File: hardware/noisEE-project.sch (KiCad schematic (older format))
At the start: 109 parts, among them IC1 ATTINY84-S, J1 VOL_CONN, J2 Stereo_CONN, J3 COLOR_CONN, J4 USB_OTG, P2 ISP_02x03, Q1 PN2222A, Q2 PN2222A, SW1 SW_DIP_x01, U1 LMH6642(SOT23)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

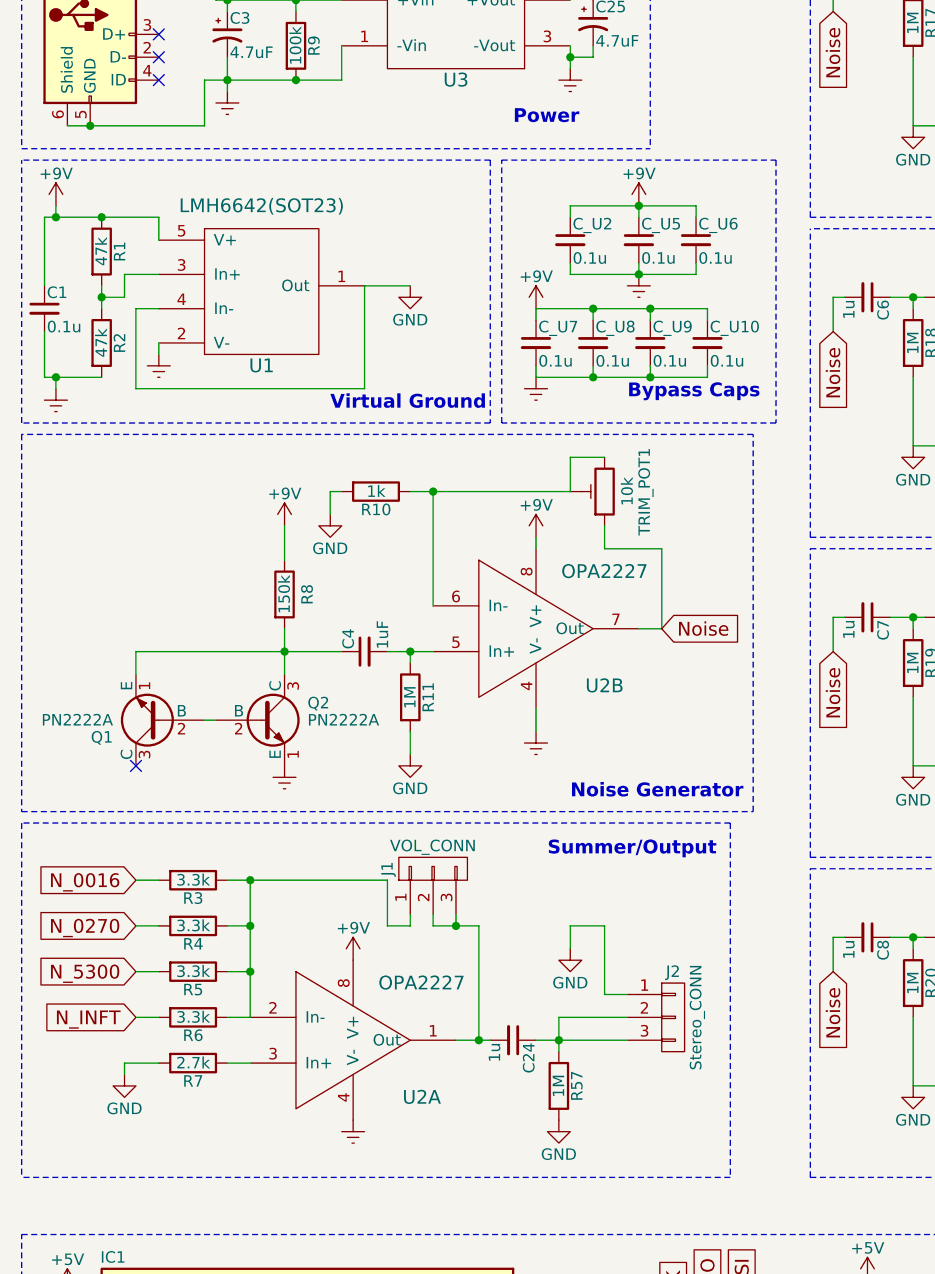
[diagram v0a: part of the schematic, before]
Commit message: Use two opamps for pre-amp and output stages, clean up board and lay down tracks for all signal paths
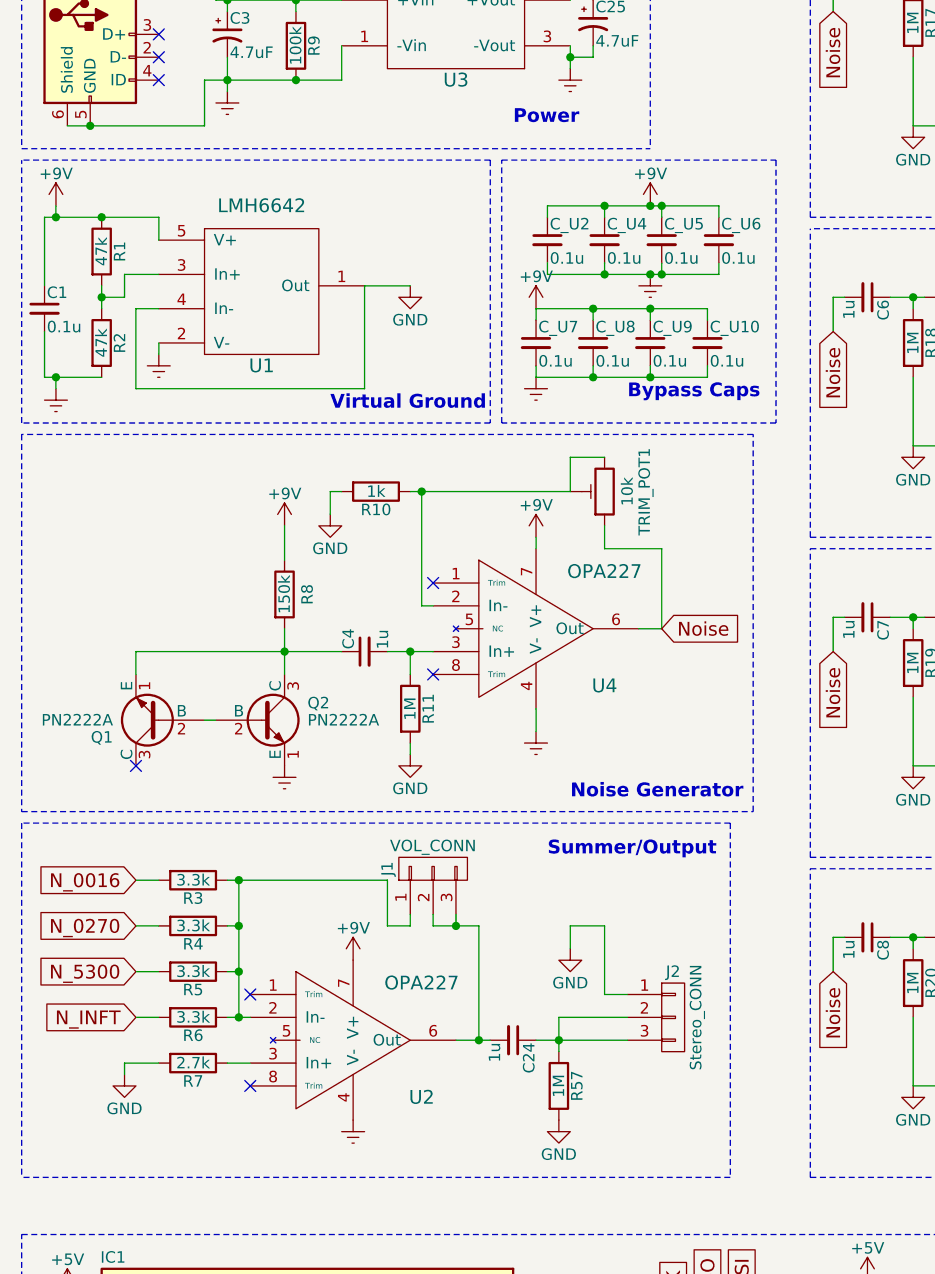
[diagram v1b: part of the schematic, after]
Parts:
- removed U2: OPA2227, Housings_SOIC:SOIC-8_3.9x4.9mm_Pitch1.27mm, symbol OPA2227
- added C_U4: 0.1u, Capacitors_SMD:C_0805, symbol C_Small
- added U2, U4: OPA227, Housings_SOIC:SOIC-8_3.9x4.9mm_Pitch1.27mm, symbol OPA227
- C4: value 1uF -> 1u
- U1: value LMH6642(SOT23) -> LMH6642
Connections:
- net +9V: now also C_U4.1, U2.7 (V+), U4.7 (V+)
- net Earth: now also C_U4.2, U2.4 (V-), U4.4 (V-)
- net Noise: now also U4.6 (Out)
- net at C4.2, R11.1: now also U4.3 (In+)
- net at R10.1, TRIM_POT1.2, TRIM_POT1.3: now also U4.2 (In-)
- net at C24.2, J1.2 (P2), J1.3 (P3): now also U2.6 (Out)
- net at J1.1 (P1), R3.1, R4.1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: now also U2.2 (In-)
- net at R7.1: now also U2.3 (In+)
- no-connect marks 4 -> 8
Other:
- moved on the sheet: C_U2, C_U5, C_U6, R11
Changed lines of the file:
@@
 P 1550 2150
 F 0 "U1" H 1550 1800 60  0000 C CNN
-F 1 "LMH6642(SOT23)" H 1550 2500 60  0000 C CNN
+F 1 "LMH6642" H 1550 2500 60  0000 C CNN
 F 2 "TO_SOT_Packages_SMD:SOT-23-5" H 1550 2150 60  0001 C CNN
 F 3 "" H 1550 2150 60  0001 C CNN
@@
 P 2000 3750
 F 0 "C4" H 2010 3820 50  0000 L CNN
-F 1 "1uF" H 2010 3670 50  0000 L CNN
+F 1 "1u" H 2010 3670 50  0000 L CNN
 F 2 "Capacitors_SMD:C_0805" H 2000 3750 50  0001 C CNN
 F 3 "" H 2000 3750 50  0000 C CNN
@@
 $EndComp
 $Comp
-L OPA2227 U2
-U 2 1 58A176E6
-P 2650 3650
-F 0 "U2" H 3050 3400 60  0000 C CNN
-F 1 "OPA2227" H 3050 3900 60  0000 C CNN
-F 2 "Housings_SOIC:SOIC-8_3.9x4.9mm_Pitch1.27mm" H 2650 3650 60  0001 C CNN
-F 3 "" H 2650 3650 60  0001 C CNN
-	2    2650 3650
-	1    0    0    -1
-$EndComp
-$Comp
 L R R10
 U 1 1 58A178E2
@@
 L R R11
 U 1 1 58A18310
-P 2200 3950
-F 0 "R11" V 2280 3950 50  0000 C CNN
-F 1 "1M" V 2200 3950 50  0000 C CNN
-F 2 "Resistors_SMD:R_0805" V 2130 3950 50  0001 C CNN
-F 3 "" H 2200 3950 50  0000 C CNN
-	1    2200 3950
+P 2200 4000
+F 0 "R11" V 2280 4000 50  0000 C CNN
+F 1 "1M" V 2200 4000 50  0000 C CNN
+F 2 "Resistors_SMD:R_0805" V 2130 4000 50  0001 C CNN
+F 3 "" H 2200 4000 50  0000 C CNN
+	1    2200 4000
 	1    0    0    -1
 $EndComp
@@
 N_0016
 $Comp
-L OPA2227 U2
-U 1 1 58A24451
-P 1850 5450
-F 0 "U2" H 2250 5200 60  0000 C CNN
-F 1 "OPA2227" H 2250 5700 60  0000 C CNN
-F 2 "Housings_SOIC:SOIC-8_3.9x4.9mm_Pitch1.27mm" H 1850 5450 60  0001 C CNN
-F 3 "" H 1850 5450 60  0001 C CNN
-	1    1850 5450
-	1    0    0    -1
-$EndComp
-$Comp
 L +9V #PWR019
 U 1 1 58A2555B
@@
 L +9V #PWR087
 U 1 1 58E53024
-P 3200 1800
-F 0 "#PWR087" H 3200 1650 50  0001 C CNN
-F 1 "+9V" H 3200 1940 50  0000 C CNN
-F 2 "" H 3200 1800 50  0000 C CNN
-F 3 "" H 3200 1800 50  0000 C CNN
-	1    3200 1800
+P 3250 1800
+F 0 "#PWR087" H 3250 1650 50  0001 C CNN
+F 1 "+9V" H 3250 1940 50  0000 C CNN
+F 2 "" H 3250 1800 50  0000 C CNN
+F 3 "" H 3250 1800 50  0000 C CNN
+	1    3250 1800
 	1    0    0    -1
 $EndComp
@@
 L Earth #PWR088
 U 1 1 58E5317F
-P 3200 2100
-F 0 "#PWR088" H 3200 1850 50  0001 C CNN
-F 1 "Earth" H 3200 1950 50  0001 C CNN
-F 2 "" H 3200 2100 50  0000 C CNN
-F 3 "" H 3200 2100 50  0000 C CNN
-	1    3200 2100
+P 3250 2100
+F 0 "#PWR088" H 3250 1850 50  0001 C CNN
+F 1 "Earth" H 3250 1950 50  0001 C CNN
+F 2 "" H 3250 2100 50  0000 C CNN
+F 3 "" H 3250 2100 50  0000 C CNN
+	1    3250 2100
 	1    0    0    -1
 $EndComp
@@
 L C_Small C_U2
 U 1 1 58E5342B
-P 2900 1950
-F 0 "C_U2" H 2910 2020 50  0000 L CNN
-F 1 "0.1u" H 2910 1870 50  0000 L CNN
-F 2 "Capacitors_SMD:C_0805" H 2900 1950 50  0001 C CNN
-F 3 "" H 2900 1950 50  0000 C CNN
-	1    2900 1950
+P 2800 1950
+F 0 "C_U2" H 2810 2020 50  0000 L CNN
+F 1 "0.1u" H 2810 1870 50  0000 L CNN
+F 2 "Capacitors_SMD:C_0805" H 2800 1950 50  0001 C CNN
+F 3 "" H 2800 1950 50  0000 C CNN
+	1    2800 1950
 	1    0    0    -1
 $EndComp
@@
 L C_Small C_U5
 U 1 1 58E5803C
-P 3200 1950
-F 0 "C_U5" H 3210 2020 50  0000 L CNN
-F 1 "0.1u" H 3210 1870 50  0000 L CNN
-F 2 "Capacitors_SMD:C_0805" H 3200 1950 50  0001 C CNN
-F 3 "" H 3200 1950 50  0000 C CNN
-	1    3200 1950
+P 3300 1950
+F 0 "C_U5" H 3310 2020 50  0000 L CNN
+F 1 "0.1u" H 3310 1870 50  0000 L CNN
+F 2 "Capacitors_SMD:C_0805" H 3300 1950 50  0001 C CNN
+F 3 "" H 3300 1950 50  0000 C CNN
+	1    3300 1950
 	1    0    0    -1
 $EndComp
@@
 L C_Small C_U6
 U 1 1 58E5F42C
-P 3450 1950
-F 0 "C_U6" H 3460 2020 50  0000 L CNN
-F 1 "0.1u" H 3460 1870 50  0000 L CNN
-F 2 "Capacitors_SMD:C_0805" H 3450 1950 50  0001 C CNN
-F 3 "" H 3450 1950 50  0000 C CNN
-	1    3450 1950
+P 3550 1950
+F 0 "C_U6" H 3560 2020 50  0000 L CNN
+F 1 "0.1u" H 3560 1870 50  0000 L CNN
+F 2 "Capacitors_SMD:C_0805" H 3550 1950 50  0001 C CNN
+F 3 "" H 3550 1950 50  0000 C CNN
+	1    3550 1950
 	1    0    0    -1
 $EndComp
@@
 Wire Wire Line
 	2200 3050 2900 3050
-Connection ~ 2300 3050
 Wire Wire Line
 	2100 3750 2300 3750
@@
 Connection ~ 2200 3750
 Wire Wire Line
-	1500 4750 1500 5350
-Wire Wire Line
-	1400 4950 1500 4950
-Connection ~ 1500 4950
-Wire Wire Line
-	1400 5150 1500 5150
-Connection ~ 1500 5150
-Wire Wire Line
 	1500 5350 1400 5350
-Connection ~ 1500 4750
 Connection ~ 2500 5450
 Wire Wire Line
@@
 Connection ~ 1700 1250
 Wire Wire Line
-	2200 3750 2200 3800
-Wire Wire Line
-	2200 4100 2200 4200
-Wire Wire Line
 	3050 3200 3050 3300
 Wire Wire Line
@@
 	2900 3050 2900 2900
 Wire Wire Line
-	2300 3050 2300 3550
-Wire Wire Line
 	4050 950  4050 800
 Wire Wire Line
@@
 	600  1850 600  2150
 Wire Wire Line
-	3200 1800 3200 1850
-Wire Wire Line
-	2900 1800 3450 1800
-Wire Wire Line
-	3450 1800 3450 1850
-Wire Wire Line
-	2900 1800 2900 1850
-Connection ~ 3200 1800
-Wire Wire Line
-	2900 2050 2900 2100
-Wire Wire Line
-	2900 2100 3450 2100
-Wire Wire Line
-	3200 2100 3200 2050
-Wire Wire Line
-	3450 2100 3450 2050
-Connection ~ 3200 2100
-Wire Wire Line
 	2750 2250 2750 2300
 Wire Wire Line
@@
 	2100 4750 2100 4950
 Wire Wire Line
-	2100 4750 1400 4750
-Wire Wire Line
 	2100 4950 2200 4950
 Wire Wire Line
@@
 Connection ~ 800  1450
 NoConn ~ 1100 1250
+$Comp
+L OPA227 U2
+U 1 1 58C4BAC6
+P 1850 5450
+F 0 "U2" H 2250 5200 60  0000 C CNN
+F 1 "OPA227" H 2250 5700 60  0000 C CNN
+F 2 "Housings_SOIC:SOIC-8_3.9x4.9mm_Pitch1.27mm" H 1850 5450 60  0001 C CNN
+F 3 "" H 1850 5450 60  0001 C CNN
+	1    1850 5450
+	1    0    0    -1
+$EndComp
+Wire Wire Line
+	2100 4750 1400 4750
+Wire Wire Line
+	1450 4750 1450 5350
+Connection ~ 1450 5350
+Connection ~ 1450 4750
+Wire Wire Line
+	1450 5150 1400 5150
+Connection ~ 1450 5150
+Wire Wire Line
+	1450 4950 1400 4950
+Connection ~ 1450 4950
+NoConn ~ 1500 5650
+NoConn ~ 1500 5250
+$Comp
+L OPA227 U4
+U 1 1 58C52F90
+P 2650 3650
+F 0 "U4" H 3050 3400 60  0000 C CNN
+F 1 "OPA227" H 3050 3900 60  0000 C CNN
+F 2 "Housings_SOIC:SOIC-8_3.9x4.9mm_Pitch1.27mm" H 2650 3650 60  0001 C CNN
+F 3 "" H 2650 3650 60  0001 C CNN
+	1    2650 3650
+	1    0    0    -1
+$EndComp
+Wire Wire Line
+	2200 3850 2200 3750
+Wire Wire Line
+	2200 4150 2200 4200
+NoConn ~ 2300 3850
+NoConn ~ 2300 3450
+Connection ~ 2250 3050
+Wire Wire Line
+	2300 3550 2250 3550
+$Comp
+L C_Small C_U4
+U 1 1 58C5D92D
+P 3050 1950
+F 0 "C_U4" H 3060 2020 50  0000 L CNN
+F 1 "0.1u" H 3060 1870 50  0000 L CNN
+F 2 "Capacitors_SMD:C_0805" H 3050 1950 50  0001 C CNN
+F 3 "" H 3050 1950 50  0001 C CNN
+	1    3050 1950
+	1    0    0    -1
+$EndComp
+Wire Wire Line
+	2800 1850 2800 1800
+Wire Wire Line
+	3550 1800 3550 1850
+Wire Wire Line
+	3300 1800 3300 1850
+Connection ~ 3250 1800
+Wire Wire Line
+	3050 1800 3050 1850
+Connection ~ 3050 1800
+Wire Wire Line
+	2800 1800 3550 1800
+Connection ~ 3300 1800
+Wire Wire Line
+	3550 2100 3550 2050
+Wire Wire Line
+	2800 2100 3550 2100
+Wire Wire Line
+	3300 2050 3300 2100
+Connection ~ 3300 2100
+Wire Wire Line
+	3050 2050 3050 2100
+Connection ~ 3250 2100
+Wire Wire Line
+	2800 2050 2800 2100
+Connection ~ 3050 2100
+Wire Wire Line
+	2250 3550 2250 3050
 $EndSCHEMATC

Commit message: Split up the ground (GND->VCOM)
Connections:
- net GND renamed VCOM

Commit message: Check in v2 hardware with fixes for USI and AD5292 Vss issues
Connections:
- net Earth: now also U10.9 (GND), U7.9 (GND), U8.9 (GND), U9.9 (GND)
- net SPI_MISO: now also R16.2; no longer R15.2, R58.2
- net SPI_MOSI: now also R15.2, R58.2; no longer R16.2
- net VCOM: no longer U10.9 (GND), U7.9 (GND), U8.9 (GND), U9.9 (GND)
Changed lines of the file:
@@
 Text GLabel 4250 6850 2    60   Input ~ 0
 SPI_CLK
+Text GLabel 4250 7250 2    60   Input ~ 0
+SPI_MISO
 Text GLabel 4250 7050 2    60   Input ~ 0
-SPI_MISO
-Text GLabel 4250 7250 2    60   Input ~ 0
 SPI_MOSI
 $Comp
@@
 $EndComp
 $Comp
-L VCOM #PWR084
-U 1 1 58CA09E1
-P 9650 1800
-F 0 "#PWR084" H 9650 1650 50  0001 C CNN
-F 1 "VCOM" H 9650 1950 50  0000 C CNN
-F 2 "" H 9650 1800 50  0001 C CNN
-F 3 "" H 9650 1800 50  0001 C CNN
-	1    9650 1800
-	-1   0    0    1
-$EndComp
-$Comp
-L VCOM #PWR085
-U 1 1 58CA247F
-P 9650 3300
-F 0 "#PWR085" H 9650 3150 50  0001 C CNN
-F 1 "VCOM" H 9650 3450 50  0000 C CNN
-F 2 "" H 9650 3300 50  0001 C CNN
-F 3 "" H 9650 3300 50  0001 C CNN
-	1    9650 3300
-	-1   0    0    1
-$EndComp
-$Comp
 L VCOM #PWR086
 U 1 1 58CA25E9
@@
 $EndComp
 $Comp
-L VCOM #PWR087
-U 1 1 58CA4755
-P 9650 4800
-F 0 "#PWR087" H 9650 4650 50  0001 C CNN
-F 1 "VCOM" H 9650 4950 50  0000 C CNN
-F 2 "" H 9650 4800 50  0001 C CNN
-F 3 "" H 9650 4800 50  0001 C CNN
-	1    9650 4800
-	-1   0    0    1
-$EndComp
-$Comp
 L VCOM #PWR088
 U 1 1 58CA48BF
@@
 $EndComp
 $Comp
-L VCOM #PWR089
-U 1 1 58CA601D
+L Earth #PWR?
+U 1 1 5947F218
 P 9650 6300
-F 0 "#PWR089" H 9650 6150 50  0001 C CNN
-F 1 "VCOM" H 9650 6450 50  0000 C CNN
+F 0 "#PWR?" H 9650 6050 50  0001 C CNN
+F 1 "Earth" H 9650 6150 50  0001 C CNN
 F 2 "" H 9650 6300 50  0001 C CNN
 F 3 "" H 9650 6300 50  0001 C CNN
 	1    9650 6300
-	-1   0    0    1
-$EndComp
-$Comp
-L VCOM #PWR090
-U 1 1 58CA6187
+	1    0    0    -1
+$EndComp
+$Comp
+L VCOM #PWR?
+U 1 1 5947F38C
 P 8300 5450
-F 0 "#PWR090" H 8300 5300 50  0001 C CNN
+F 0 "#PWR?" H 8300 5300 50  0001 C CNN
 F 1 "VCOM" H 8300 5600 50  0000 C CNN
 F 2 "" H 8300 5450 50  0001 C CNN
@@
 	-1   0    0    1
 $EndComp
+$Comp
+L Earth #PWR?
+U 1 1 594A0FDF
+P 9650 4800
+F 0 "#PWR?" H 9650 4550 50  0001 C CNN
+F 1 "Earth" H 9650 4650 50  0001 C CNN
+F 2 "" H 9650 4800 50  0001 C CNN
+F 3 "" H 9650 4800 50  0001 C CNN
+	1    9650 4800
+	1    0    0    -1
+$EndComp
+$Comp
+L Earth #PWR?
+U 1 1 594A1BD5
+P 9650 3300
+F 0 "#PWR?" H 9650 3050 50  0001 C CNN
+F 1 "Earth" H 9650 3150 50  0001 C CNN
+F 2 "" H 9650 3300 50  0001 C CNN
+F 3 "" H 9650 3300 50  0001 C CNN
+	1    9650 3300
+	1    0    0    -1
+$EndComp
+$Comp
+L Earth #PWR?
+U 1 1 594A299F
+P 9650 1800
+F 0 "#PWR?" H 9650 1550 50  0001 C CNN
+F 1 "Earth" H 9650 1650 50  0001 C CNN
+F 2 "" H 9650 1800 50  0001 C CNN
+F 3 "" H 9650 1800 50  0001 C CNN
+	1    9650 1800
+	1    0    0    -1
+$EndComp
 $EndSCHEMATC
